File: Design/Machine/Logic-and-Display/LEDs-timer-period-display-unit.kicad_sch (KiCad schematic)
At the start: 0 parts

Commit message: feat: schematics w/out buzzer, some LEDS, matrix
add schematics for LEDs and time display, missing FC-16 module (8x32 matrix) connection, left priority, right side LEDS, and buzzer
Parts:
- added A1: Arduino_Nano_v3.x, Module:Arduino_Nano, symbol MCU_Module:Arduino_Nano_v3.x
- added D1: Blue 5mm, symbol Device:LED
- added D2, D5, D6: Red 5mm, symbol Device:LED
- added D3, D4: Yellow 5mm, symbol Device:LED
- added R1, R10, R11, R2, R3, R4, R5, R6, R7: 220, symbol Device:R
- added R12, R13, R8, R9: 330, symbol Device:R
- added U1: 4511, symbol 4xxx_IEEE:4511
- added U2: Red, symbol Arduino modules:HSN8011AUR
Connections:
- new net: R2.1, U2.12 (b)
- new net: R2.2, U1.12 (Qb)
- new net: D4.1 (K), R11.1
- new net: A1.11 (D8), D3.2 (A), D4.2 (A)
- new net: R1.1, U2.1 (a)
- new net: R1.2, U1.13 (Qa)
- new net: D2.1 (K), R9.1
- new net: R3.1, U2.10 (c)
- new net: R3.2, U1.11 (Qc)
- new net: R5.1, U2.4 (e)
- new net: R5.2, U1.9 (Qe)
- new net: D3.1 (K), R10.1
- new net: D5.1 (K), R12.1
- new net: A1.10 (D7), D2.2 (A)
- new net: A1.12 (D9), D5.2 (A), D6.2 (A)
- new net: A1.5 (D2), U1.7 (DA)
- new net: A1.6 (D3), U1.1 (DB)
- new net: A1.7 (D4), U1.2 (DC)
- new net: A1.8 (D5), U1.6 (DD)
- new net: A1.9 (D6), D1.2 (A)
- new net: R4.2, U1.10 (Qd)
- new net: R7.2, U1.14 (Qg)
- new net: R6.2, U1.15 (Qf)
- new net: D6.1 (K), R13.1
- new net: R6.1, U2.2 (f)
- new net: R4.1, U2.8 (d)
- new net: D1.1 (K), R8.1
- new net: R7.1, U2.11 (g)
- new net +5V: A1.30 (VIN), U1.16 (Vdd), U1.3 (~{LT}), U1.4 (~{BI})
- new net ESP32-TX0: A1.2 (D0/RX)
- new net GND: A1.29 (GND), A1.4 (GND), R10.2, R11.2, R12.2, R13.2, R8.2, R9.2, U1.5 (~{EL}), U1.8 (Vss), U2.13 (GND), U2.3 (GND), U2.5 (GND), U2.9 (GND)
- no-connect marks 0 -> 12

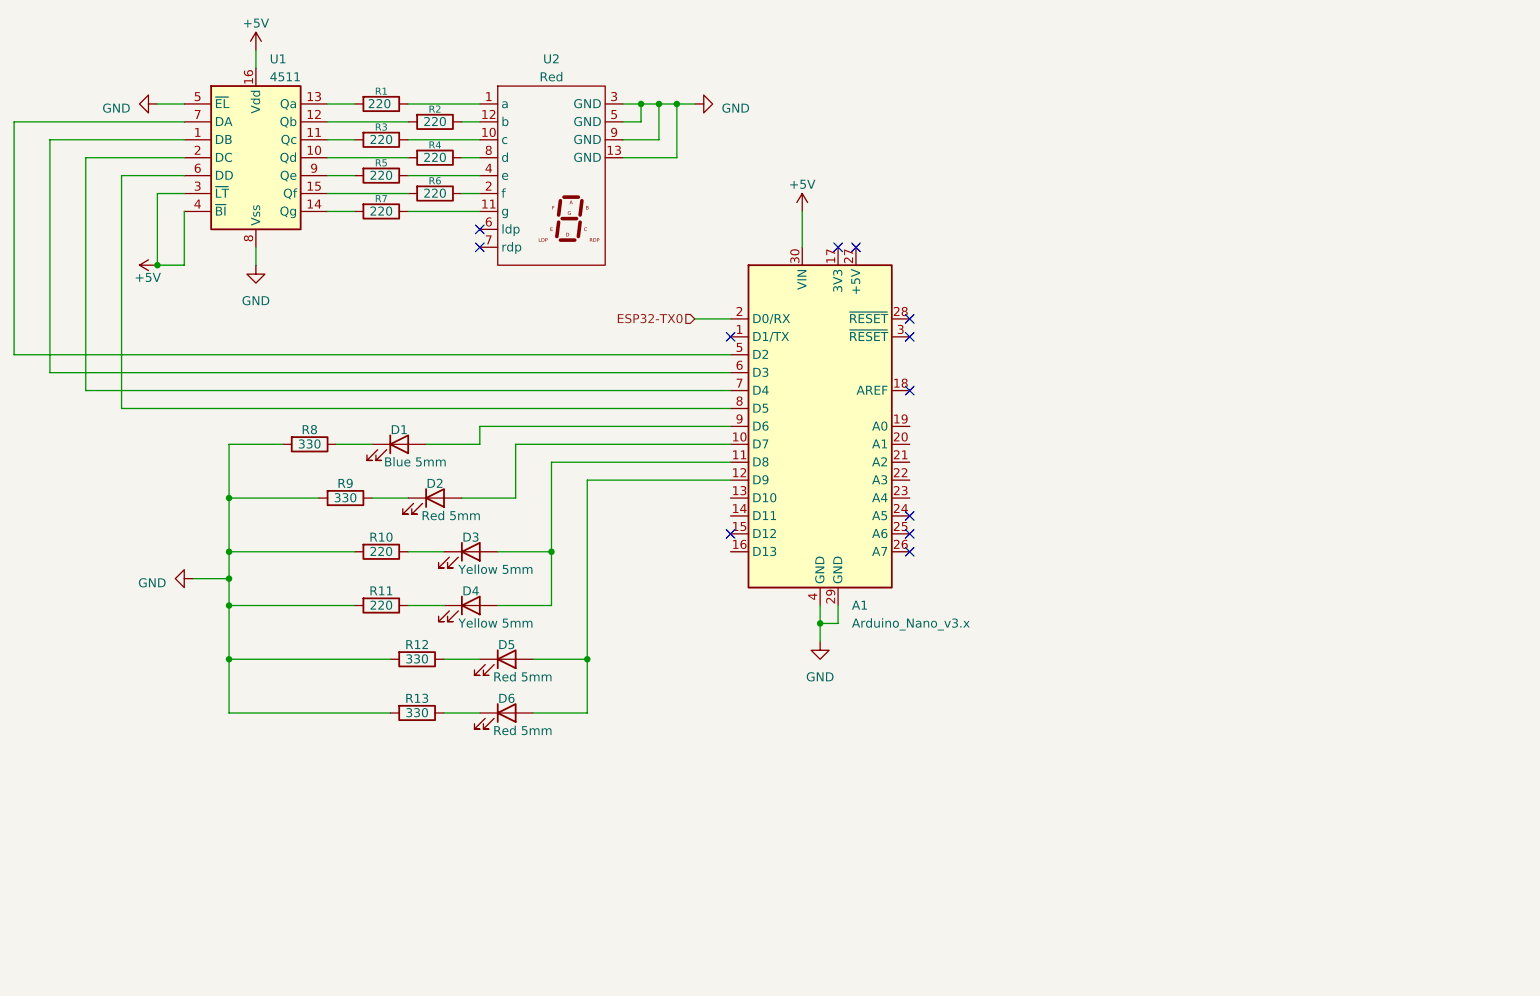
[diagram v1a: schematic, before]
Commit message: feat: display units schematics
complete all display units schematics, this is left and right scores units; and LEDs, timer, and period display unit
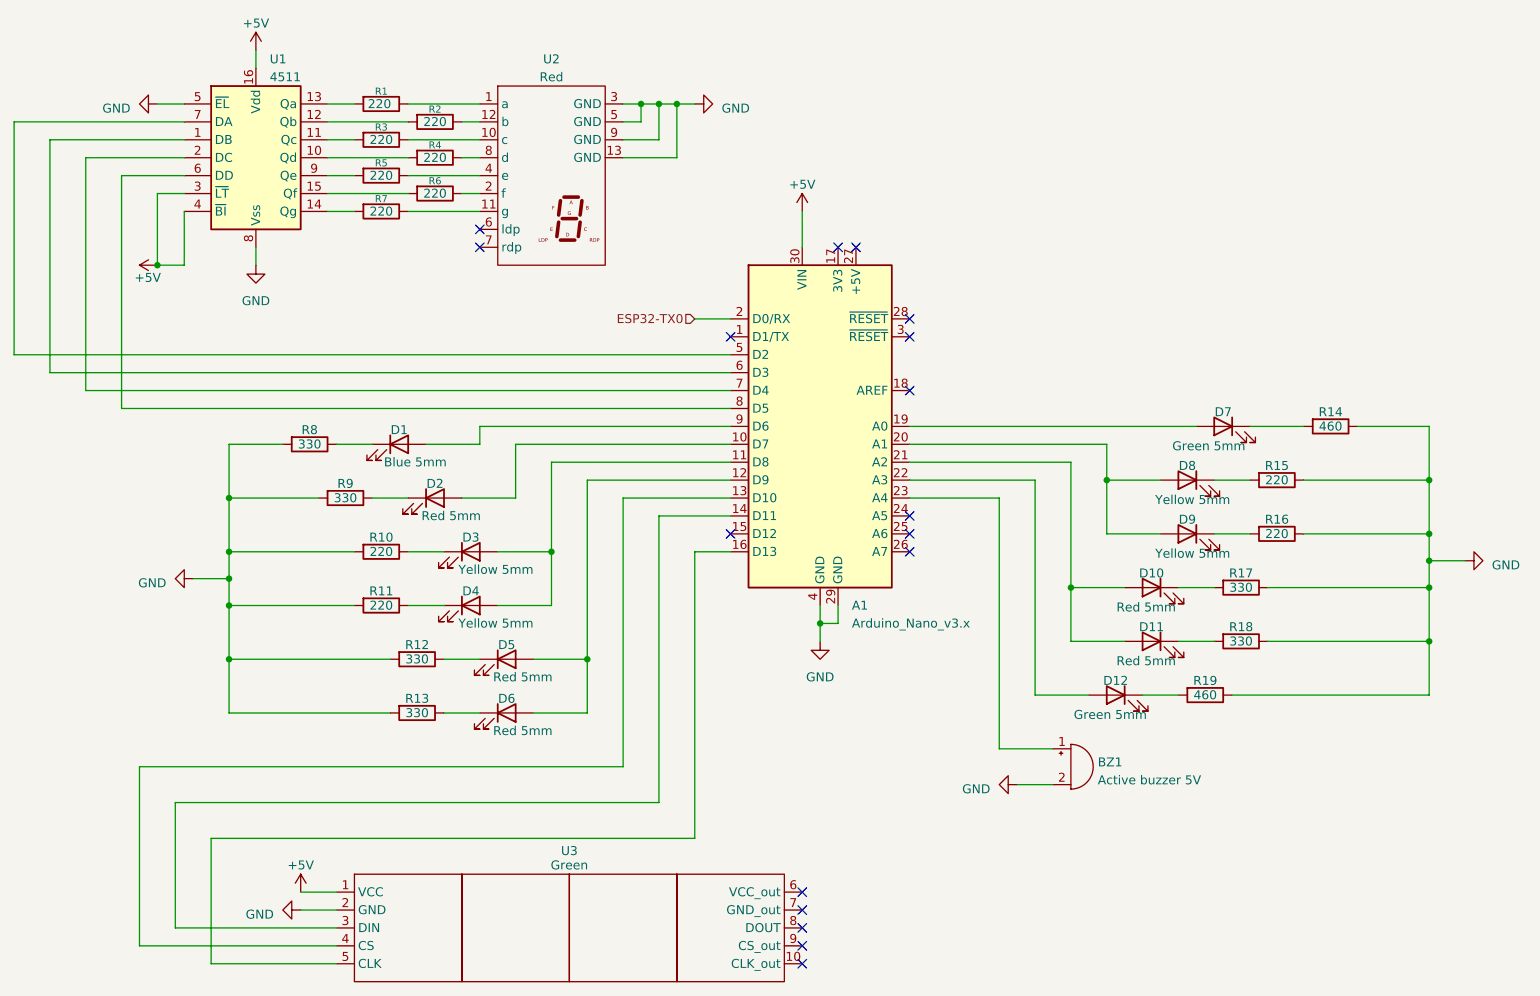
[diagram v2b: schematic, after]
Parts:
- added BZ1: Active buzzer 5V, Connector_PinSocket_2.54mm:PinSocket_1x02_P2.54mm_Vertical, symbol Device:Buzzer
- added D10, D11: Red 5mm, Connector_PinSocket_2.54mm:PinSocket_1x02_P2.54mm_Vertical, symbol Device:LED
- added D12, D7: Green 5mm, Connector_PinSocket_2.54mm:PinSocket_1x02_P2.54mm_Vertical, symbol Device:LED
- added D8, D9: Yellow 5mm, Connector_PinSocket_2.54mm:PinSocket_1x02_P2.54mm_Vertical, symbol Device:LED
- added R14, R19: 460, Resistor_THT:R_Axial_DIN0309_L9.0mm_D3.2mm_P15.24mm_Horizontal, symbol Device:R
- added R15, R16: 220, Resistor_THT:R_Axial_DIN0309_L9.0mm_D3.2mm_P15.24mm_Horizontal, symbol Device:R
- added R17, R18: 330, Resistor_THT:R_Axial_DIN0309_L9.0mm_D3.2mm_P15.24mm_Horizontal, symbol Device:R
- added U3: Green, Connector_PinSocket_2.54mm:PinSocket_1x05_P2.54mm_Vertical, symbol Arduino modules:FC-16_32x8_LED_matrix_MAX7219
- D1, D2, D3, D4, D5, D6: footprint (none) -> Connector_PinSocket_2.54mm:PinSocket_1x02_P2.54mm_Vertical
- R1, R10, R11, R12, R13, R2, R3, R4, R5, R6, R7, R8, R9: footprint (none) -> Resistor_THT:R_Axial_DIN0309_L9.0mm_D3.2mm_P15.24mm_Horizontal
- U1: footprint (none) -> Socket:DIP_Socket-16_W4.3_W5.08_W7.62_W10.16_W10.9_3M_216-3340-00-0602J
- U2: footprint (none) -> Connector_PinSocket_2.54mm:PinSocket_1x13_P2.54mm_Vertical
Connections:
- net +5V: now also U3.1 (VCC)
- net GND: now also BZ1.2 (+), R14.1, R15.1, R16.1, R17.1, R18.1, R19.1, U3.2 (GND)
- net at A1.13 (D10): now also U3.4 (CS)
- net at A1.14 (D11): now also U3.3 (DIN)
- net at A1.16 (D13): now also U3.5 (CLK)
- net at A1.19 (A0): now also D7.2 (A)
- net at A1.20 (A1): now also D8.2 (A), D9.2 (A)
- net at A1.21 (A2): now also D10.2 (A), D11.2 (A)
- net at A1.22 (A3): now also D12.2 (A)
- net at A1.23 (A4): now also BZ1.1 (-)
- new net: D10.1 (K), R17.2
- new net: D11.1 (K), R18.2
- new net: D9.1 (K), R16.2
- new net: D12.1 (K), R19.2
- new net: D8.1 (K), R15.2
- new net: D7.1 (K), R14.2
- no-connect marks 12 -> 17
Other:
- title: (none) -> LEDs, timer, and period display unit schematic

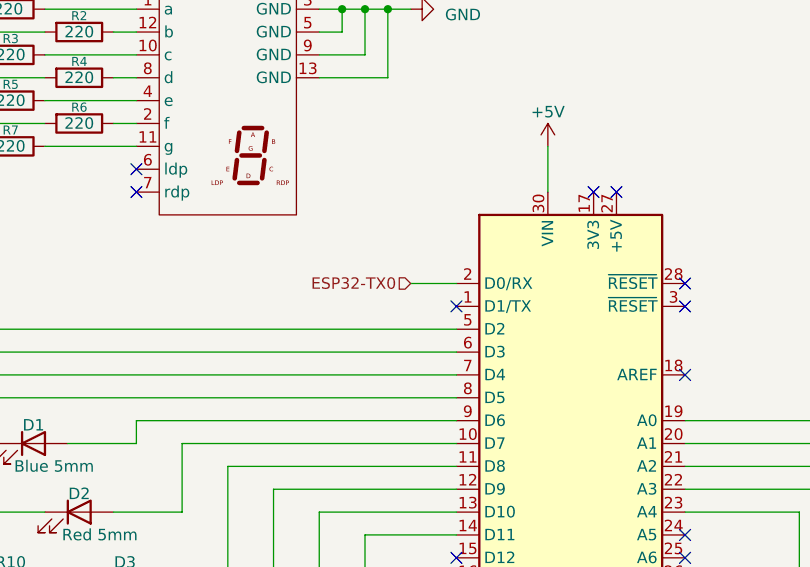
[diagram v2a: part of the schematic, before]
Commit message: feat: logic unit schematics
make schematics for logic unit, power redundancy unit still missing
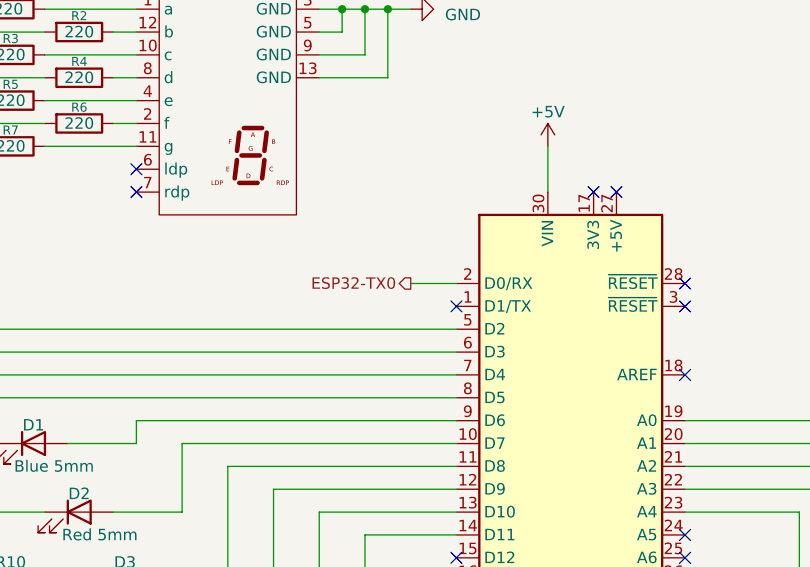
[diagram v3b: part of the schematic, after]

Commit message: feat: logic and display units schecmatics
complete logic and display units schematics
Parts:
- U1: footprint Socket:DIP_Socket-16_W4.3_W5.08_W7.62_W10.16_W10.9_3M_216-3340-00-0602J -> Package_DIP:DIP-16_W7.62mm
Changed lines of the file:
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@@
       (effects (font (size 1.27 1.27)) (justify left))
     )
-    (property "Footprint" "Socket:DIP_Socket-16_W4.3_W5.08_W7.62_W10.16_W10.9_3M_216-3340-00-0602J" (at 57.15 55.88 0)
+    (property "Footprint" "Package_DIP:DIP-16_W7.62mm" (at 57.15 55.88 0)
       (effects (font (size 1.27 1.27)) hide)
     )
